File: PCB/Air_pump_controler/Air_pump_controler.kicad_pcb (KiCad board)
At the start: 2 copper layers, 24 x 24 mm, 29 parts, among them J1 Conn_01x03_Pin, J2 USB IN, J4 Motor_conn, Q1 AP30N03DF, U1 CH32V003F4U6

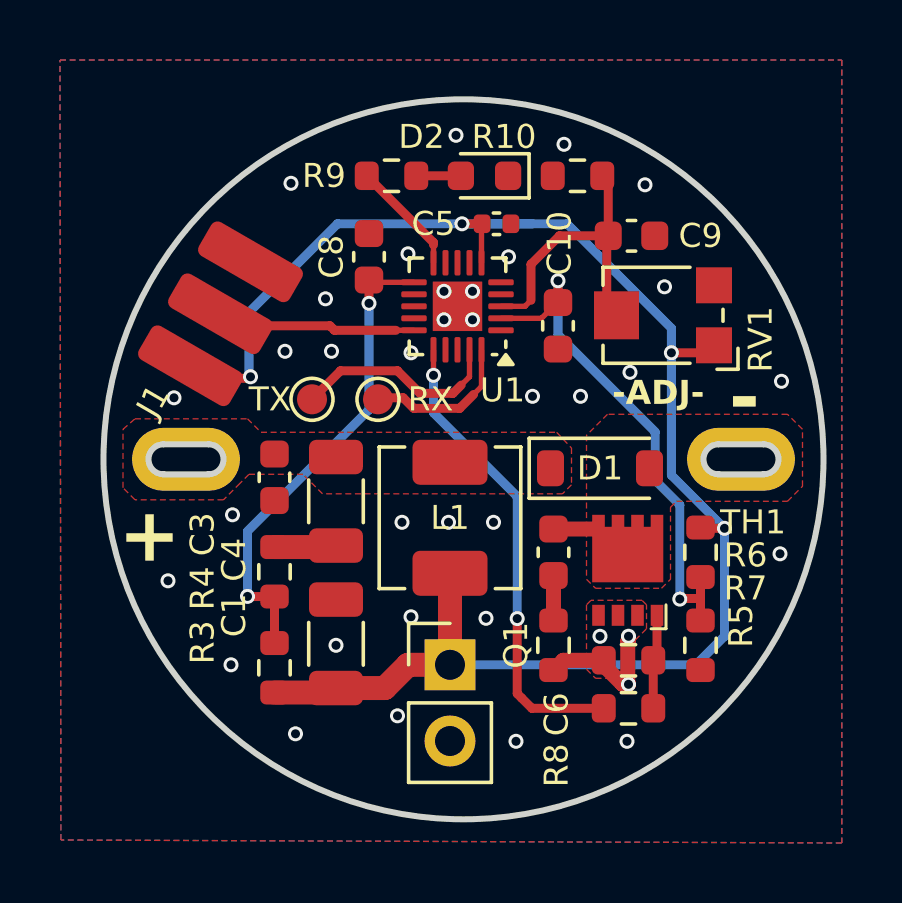
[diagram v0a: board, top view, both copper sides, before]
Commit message: Update
changed potenciometer voltage divider, added filter cap
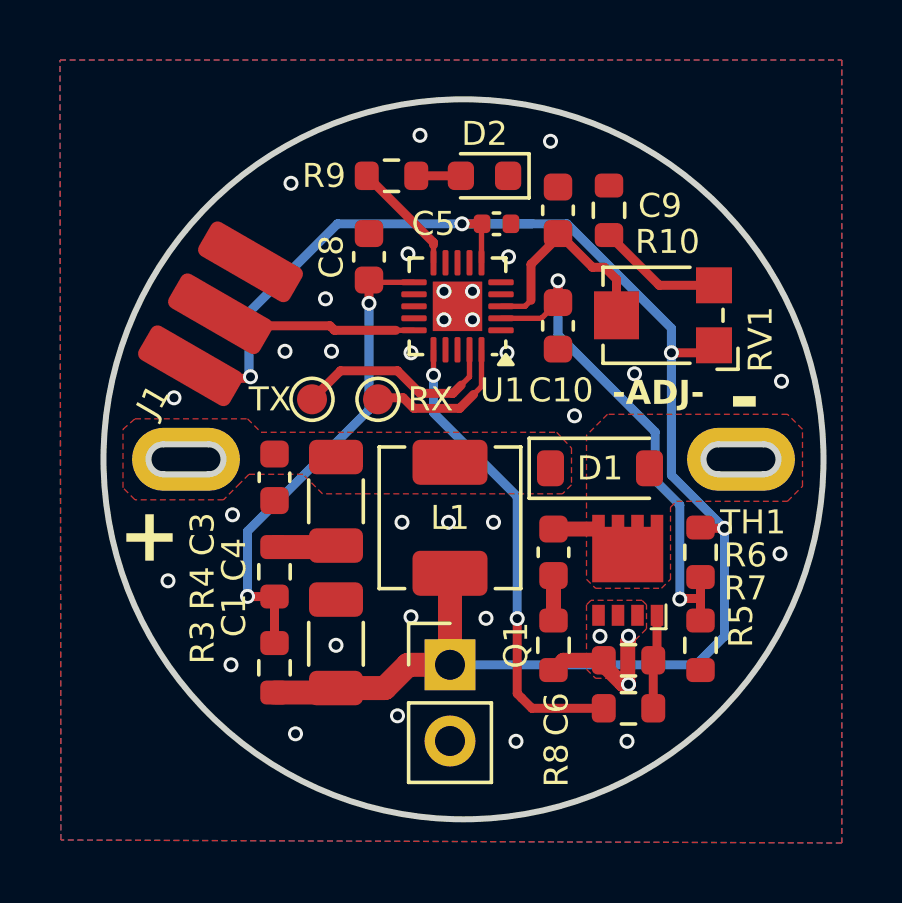
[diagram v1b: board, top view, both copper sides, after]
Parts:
- R10: value 2k -> 20k
- moved C9 2.59 mm to (160.6, 81.0), turned to 90 degrees
- moved R10 1.56 mm to (162.2, 81.0), turned to -90 degrees
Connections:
- R10 pad 2: /AN_POT -> Net-(R10-Pad2)
- RV1 pad 3: unconnected-(RV1-Pad3) -> Net-(R10-Pad2)
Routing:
- net Net-(R10-Pad2): track 0.00 -> 4.19 mm
- net /AN_POT: track 10.1 -> 8.20 mm
- net GND: vias 37 -> 35
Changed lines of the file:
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@@
 	(net 24 "unconnected-(U1-PD4-Pad18)")
 	(net 25 "unconnected-(U1-PD3-Pad17)")
-	(net 26 "unconnected-(RV1-Pad3)")
+	(net 26 "Net-(R10-Pad2)")
 	(footprint "Potentiometer_SMD:Potentiometer_Bourns_TC33X_Vertical"
 		(layer "F.Cu")
@@
 			(size 1.2 1.2)
 			(layers "F.Cu" "F.Mask" "F.Paste")
-			(net 26 "unconnected-(RV1-Pad3)")
+			(net 26 "Net-(R10-Pad2)")
 			(pinfunction "3")
-			(pintype "passive+no_connect")
+			(pintype "passive")
 		)
 		(embedded_fonts no)
@@
 		(tags "capacitor")
 		(property "Reference" "C10"
-			(at -2.75 -0.05 90)
+			(at 2.15 -0.1 180)
 			(layer "F.SilkS")
 			(effects
@@
 	(footprint "Capacitor_SMD:C_0603_1608Metric"
 		(layer "F.Cu")
-		(at 163 81.85)
+		(at 160.55 81 90)
 		(descr "Capacitor SMD 0603 (1608 Metric), square (rectangular) end terminal, IPC-7351 nominal, (Body size source: IPC-SM-782 page 76, https://www.pcb-3d.com/wordpress/wp-content/uploads/ipc-sm-782a_amendment_1_and_2.pdf), generated with kicad-footprint-generator")
 		(tags "capacitor")
 		(property "Reference" "C9"
-			(at 2.3 0 180)
+			(at 0.15 3.4 180)
 			(layer "F.SilkS")
 			(effects
@@
 		)
 		(property "Value" "100nF"
-			(at 0 1.43 0)
+			(at 0 1.43 90)
 			(layer "F.Fab")
 			(effects
@@
 		)
 		(property "Datasheet" ""
-			(at 0 0 0)
+			(at 0 0 90)
 			(layer "F.Fab")
 			(hide yes)
@@
 		)
 		(property "Description" ""
-			(at 0 0 0)
+			(at 0 0 90)
 			(layer "F.Fab")
 			(hide yes)
@@
 		)
 		(fp_line
-			(start -1.48 -0.73)
-			(end 1.48 -0.73)
+			(start 1.48 -0.73)
+			(end 1.48 0.73)
 			(stroke
 				(width 0.05)
@@
 		)
 		(fp_line
-			(start -1.48 0.73)
-			(end -1.48 -0.73)
+			(start -1.48 -0.73)
+			(end 1.48 -0.73)
 			(stroke
 				(width 0.05)
@@
 		)
 		(fp_line
-			(start 1.48 -0.73)
-			(end 1.48 0.73)
+			(start 1.48 0.73)
+			(end -1.48 0.73)
 			(stroke
 				(width 0.05)
@@
 		)
 		(fp_line
-			(start 1.48 0.73)
-			(end -1.48 0.73)
+			(start -1.48 0.73)
+			(end -1.48 -0.73)
 			(stroke
 				(width 0.05)
@@
 		)
 		(fp_line
-			(start -0.8 -0.4)
-			(end 0.8 -0.4)
+			(start 0.8 -0.4)
+			(end 0.8 0.4)
 			(stroke
 				(width 0.1)
@@
 		)
 		(fp_line
-			(start -0.8 0.4)
-			(end -0.8 -0.4)
+			(start -0.8 -0.4)
+			(end 0.8 -0.4)
 			(stroke
 				(width 0.1)
@@
 		)
 		(fp_line
-			(start 0.8 -0.4)
-			(end 0.8 0.4)
+			(start 0.8 0.4)
+			(end -0.8 0.4)
 			(stroke
 				(width 0.1)
@@
 		)
 		(fp_line
-			(start 0.8 0.4)
-			(end -0.8 0.4)
+			(start -0.8 0.4)
+			(end -0.8 -0.4)
 			(stroke
 				(width 0.1)
@@
 		)
 		(fp_text user "${REFERENCE}"
-			(at 0 0 0)
+			(at 0 0 90)
 			(layer "F.Fab")
 			(effects
@@
 		)
 		(pad "1" smd roundrect
-			(at -0.775 0)
+			(at -0.775 0 90)
 			(size 0.9 0.95)
 			(layers "F.Cu" "F.Mask" "F.Paste")
@@
 		)
 		(pad "2" smd roundrect
-			(at 0.775 0)
+			(at 0.775 0 90)
 			(size 0.9 0.95)
 			(layers "F.Cu" "F.Mask" "F.Paste")
@@
 		(tags "LED")
 		(property "Reference" "D2"
-			(at 2.1 1.3 0)
+			(at 0 1.4 0)
 			(layer "F.SilkS")
 			(effects
@@
 	(footprint "Resistor_SMD:R_0603_1608Metric"
 		(layer "F.Cu")
-		(at 161.2 79.85)
+		(at 162.25 81 -90)
 		(descr "Resistor SMD 0603 (1608 Metric), square (rectangular) end terminal, IPC-7351 nominal, (Body size source: IPC-SM-782 page 72, https://www.pcb-3d.com/wordpress/wp-content/uploads/ipc-sm-782a_amendment_1_and_2.pdf), generated with kicad-footprint-generator")
 		(tags "resistor")
 		(property "Reference" "R10"
-			(at -2.45 -1.3 0)
+			(at 1.05 -1.95 180)
 			(layer "F.SilkS")
 			(effects
@@
 			)
 		)
-		(property "Value" "2k"
-			(at 0 1.43 0)
+		(property "Value" "20k"
+			(at 0 1.43 90)
 			(layer "F.Fab")
 			(effects
@@
 		)
 		(property "Datasheet" ""
-			(at 0 0 0)
+			(at 0 0 90)
 			(layer "F.Fab")
 			(hide yes)
@@
 		)
 		(property "Description" ""
-			(at 0 0 0)
+			(at 0 0 90)
 			(layer "F.Fab")
 			(hide yes)
@@
 		(attr smd)
 		(fp_line
-			(start -0.237258 -0.5225)
-			(end 0.237258 -0.5225)
+			(start -0.237258 0.5225)
+			(end 0.237258 0.5225)
 			(stroke
 				(width 0.12)
@@
 		)
 		(fp_line
-			(start -0.237258 0.5225)
-			(end 0.237258 0.5225)
+			(start -0.237258 -0.5225)
+			(end 0.237258 -0.5225)
 			(stroke
 				(width 0.12)
@@
 		)
 		(fp_line
-			(start -1.48 -0.73)
-			(end 1.48 -0.73)
+			(start -1.48 0.73)
+			(end -1.48 -0.73)
 			(stroke
 				(width 0.05)
@@
 		)
 		(fp_line
-			(start -1.48 0.73)
-			(end -1.48 -0.73)
+			(start 1.48 0.73)
+			(end -1.48 0.73)
 			(stroke
 				(width 0.05)
@@
 		)
 		(fp_line
-			(start 1.48 -0.73)
-			(end 1.48 0.73)
+			(start -1.48 -0.73)
+			(end 1.48 -0.73)
 			(stroke
 				(width 0.05)
@@
 		)
 		(fp_line
-			(start 1.48 0.73)
-			(end -1.48 0.73)
+			(start 1.48 -0.73)
+			(end 1.48 0.73)
 			(stroke
 				(width 0.05)
@@
 		)
 		(fp_line
-			(start -0.8 -0.4125)
-			(end 0.8 -0.4125)
+			(start -0.8 0.4125)
+			(end -0.8 -0.4125)
 			(stroke
 				(width 0.1)
@@
 		)
 		(fp_line
-			(start -0.8 0.4125)
-			(end -0.8 -0.4125)
+			(start 0.8 0.4125)
+			(end -0.8 0.4125)
 			(stroke
 				(width 0.1)
@@
 		)
 		(fp_line
-			(start 0.8 -0.4125)
-			(end 0.8 0.4125)
+			(start -0.8 -0.4125)
+			(end 0.8 -0.4125)
 			(stroke
 				(width 0.1)
@@
 		)
 		(fp_line
-			(start 0.8 0.4125)
-			(end -0.8 0.4125)
+			(start 0.8 -0.4125)
+			(end 0.8 0.4125)
 			(stroke
 				(width 0.1)
@@
 		)
 		(fp_text user "${REFERENCE}"
-			(at 0 0 0)
+			(at 0 0 90)
 			(layer "F.Fab")
 			(effects
@@
 		)
 		(pad "1" smd roundrect
-			(at -0.825 0)
+			(at -0.825 0 270)
 			(size 0.8 0.95)
 			(layers "F.Cu" "F.Mask" "F.Paste")
@@
 		)
 		(pad "2" smd roundrect
-			(at 0.825 0)
+			(at 0.825 0 270)
 			(size 0.8 0.95)
 			(layers "F.Cu" "F.Mask" "F.Paste")
 			(roundrect_rratio 0.25)
-			(net 12 "/AN_POT")
+			(net 26 "Net-(R10-Pad2)")
 			(pintype "passive")
 		)
@@
 	)
 	(via
-		(at 162.95 86.4)
+		(at 163.1 86.45)
 		(size 0.5)
 		(drill 0.3)
@@
 	)
 	(via
-		(at 160.75 78.8)
-		(size 0.5)
-		(drill 0.3)
-		(layers "F.Cu" "B.Cu")
-		(free yes)
-		(net 9)
-	)
-	(via
 		(at 162.85 98.7)
 		(size 0.5)
@@
 	)
 	(via
-		(at 164.1 83.55)
-		(size 0.5)
-		(drill 0.3)
-		(layers "F.Cu" "B.Cu")
-		(free yes)
-		(net 9)
-	)
-	(via
 		(at 162.9 96.8)
 		(size 0.5)
@@
 	)
 	(via
-		(at 161.3 87.2)
+		(at 158.85 85.75)
 		(size 0.5)
 		(drill 0.3)
@@
 	)
 	(via
-		(at 163.45 80.15)
-		(size 0.5)
-		(drill 0.3)
-		(layers "F.Cu" "B.Cu")
-		(free yes)
-		(net 9)
-	)
-	(via
 		(at 151.65 80.1)
 		(size 0.5)
@@
 	)
 	(via
-		(at 157.15 78.5)
+		(at 155.95 78.5)
 		(size 0.5)
 		(drill 0.3)
@@
 	)
 	(via
-		(at 159.7 87.2)
+		(at 161.1 87.85)
 		(size 0.5)
 		(drill 0.3)
@@
 		(net 9)
 	)
+	(via
+		(at 160.3 78.7)
+		(size 0.5)
+		(drill 0.3)
+		(layers "F.Cu" "B.Cu")
+		(free yes)
+		(net 9)
+	)
 	(segment
 		(start 159.65 84)
@@
 	)
 	(segment
-		(start 162.175 84.475)
-		(end 162.175 82.05)
+		(start 160.575 81.775)
+		(end 161.7 82.9)
+		(width 0.3)
+		(layer "F.Cu")
+		(net 12)
+	)
+	(segment
+		(start 162.5 83.3)
+		(end 162.5 84.5)
 		(width 0.3)
 		(layer "F.Cu")
@@
 	)
 	(segment
-		(start 160.6 81.85)
-		(end 161.925 81.85)
+		(start 161.7 82.9)
+		(end 162.1 82.9)
+		(width 0.3)
+		(layer "F.Cu")
+		(net 12)
+	)
+	(segment
+		(start 162.1 82.9)
+		(end 162.5 83.3)
 		(width 0.3)
 		(layer "F.Cu")
@@
 	)
 	(segment
-		(start 162.225 81.85)
-		(end 162.225 80.05)
+		(start 160.55 81.775)
+		(end 160.575 81.775)
 		(width 0.3)
 		(layer "F.Cu")
@@
 	)
 	(segment
-		(start 162.225 80.05)
-		(end 162.025 79.85)
+		(start 160.725 81.775)
+		(end 160.55 81.775)
 		(width 0.3)
 		(layer "F.Cu")
@@
 		(net 23)
 	)
+	(segment
+		(start 163.925 83.5)
+		(end 162.25 81.825)
+		(width 0.3)
+		(layer "F.Cu")
+		(net 26)
+	)
+	(segment
+		(start 165.75 83.5)
+		(end 163.925 83.5)
+		(width 0.3)
+		(layer "F.Cu")
+		(net 26)
+	)
 	(zone

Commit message: Update
added filter cap on input
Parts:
- added C11: 10nF, Capacitor_SMD:C_0402_1005Metric, F.Cu at (153.7, 98.8)
- added C12: 10nF, Capacitor_SMD:C_0402_1005Metric, F.Cu at (152.6, 98.8)
- added C13: 10nF, Capacitor_SMD:C_0402_1005Metric, F.Cu at (156.2, 81.5)
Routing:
- net +5V: track 56.7 -> 59.9 mm
- net GND: track 7.08 -> 8.65 mm
- net /LED: track 3.95 -> 4.48 mm
